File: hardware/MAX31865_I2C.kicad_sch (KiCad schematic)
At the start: 38 parts, among them J1 Conn_01x08, J2 AVR-ISP-6, J3 Conn_02x04_Odd_Even, J4 Conn_02x04_Odd_Even, J5 Conn_02x02_Odd_Even, U1 ATmega48A-A, Y1 16MHz

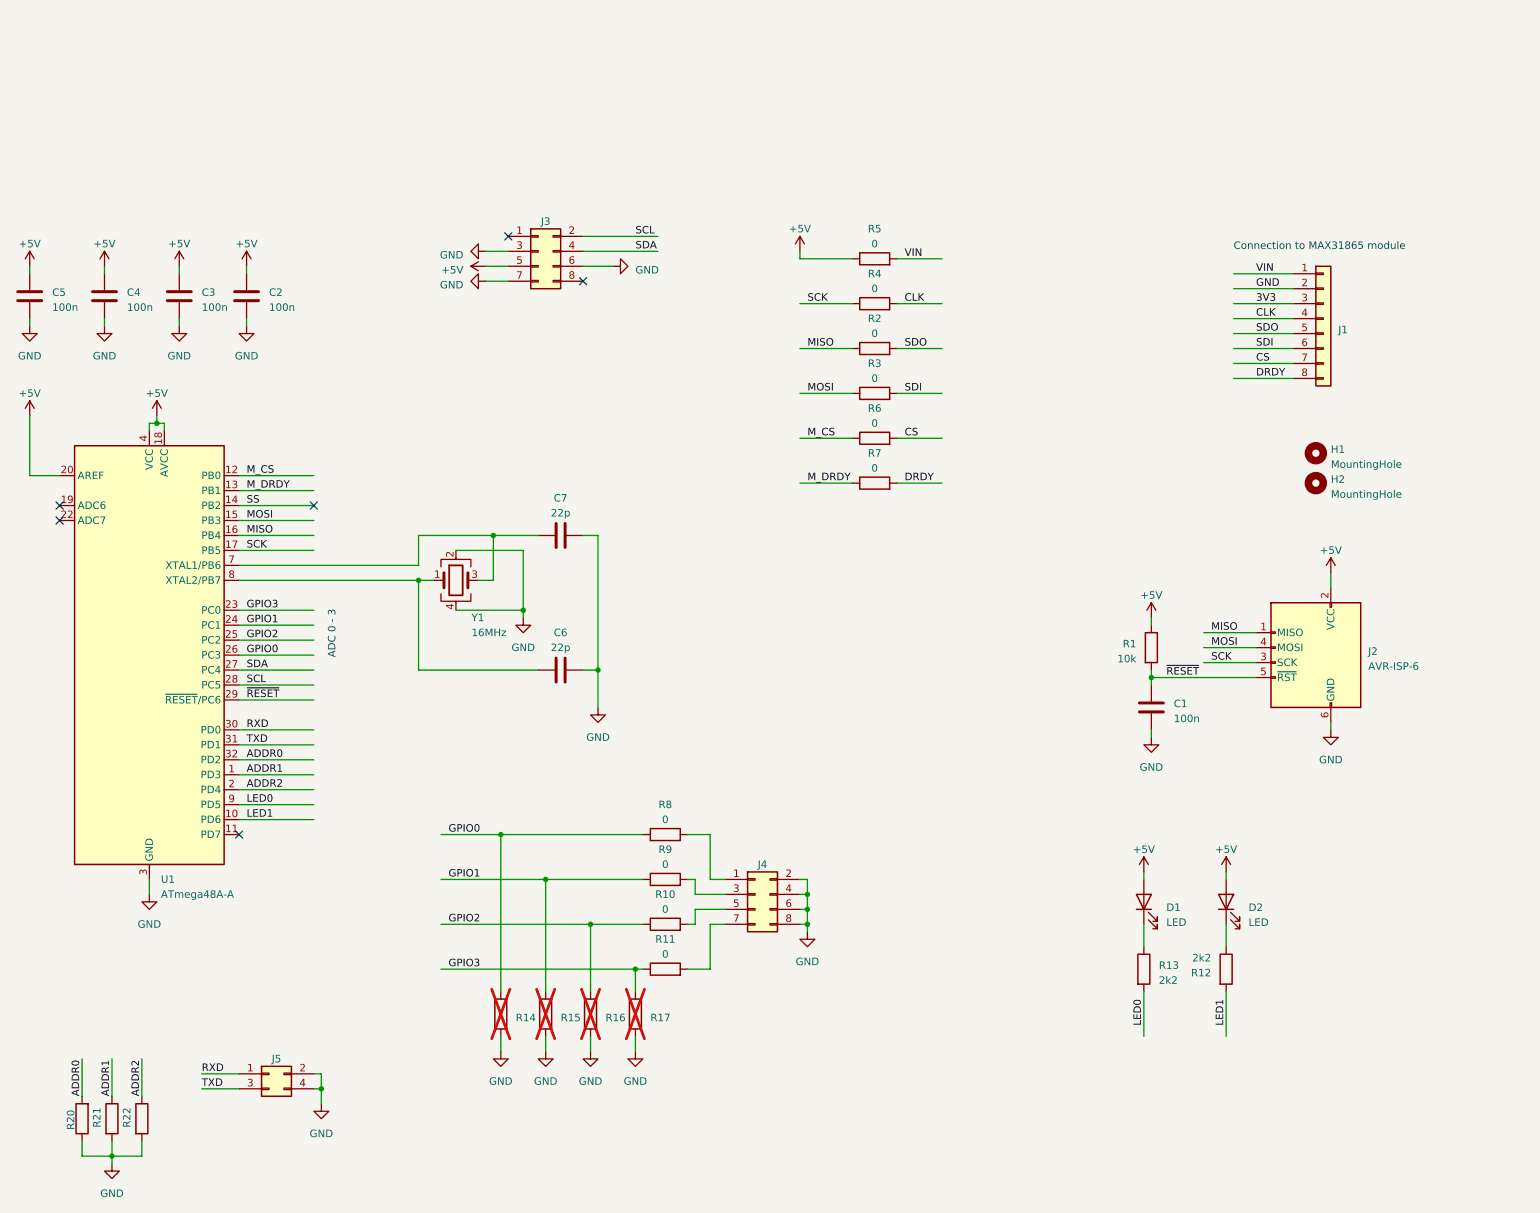
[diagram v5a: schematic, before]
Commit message: added some comments to schematic
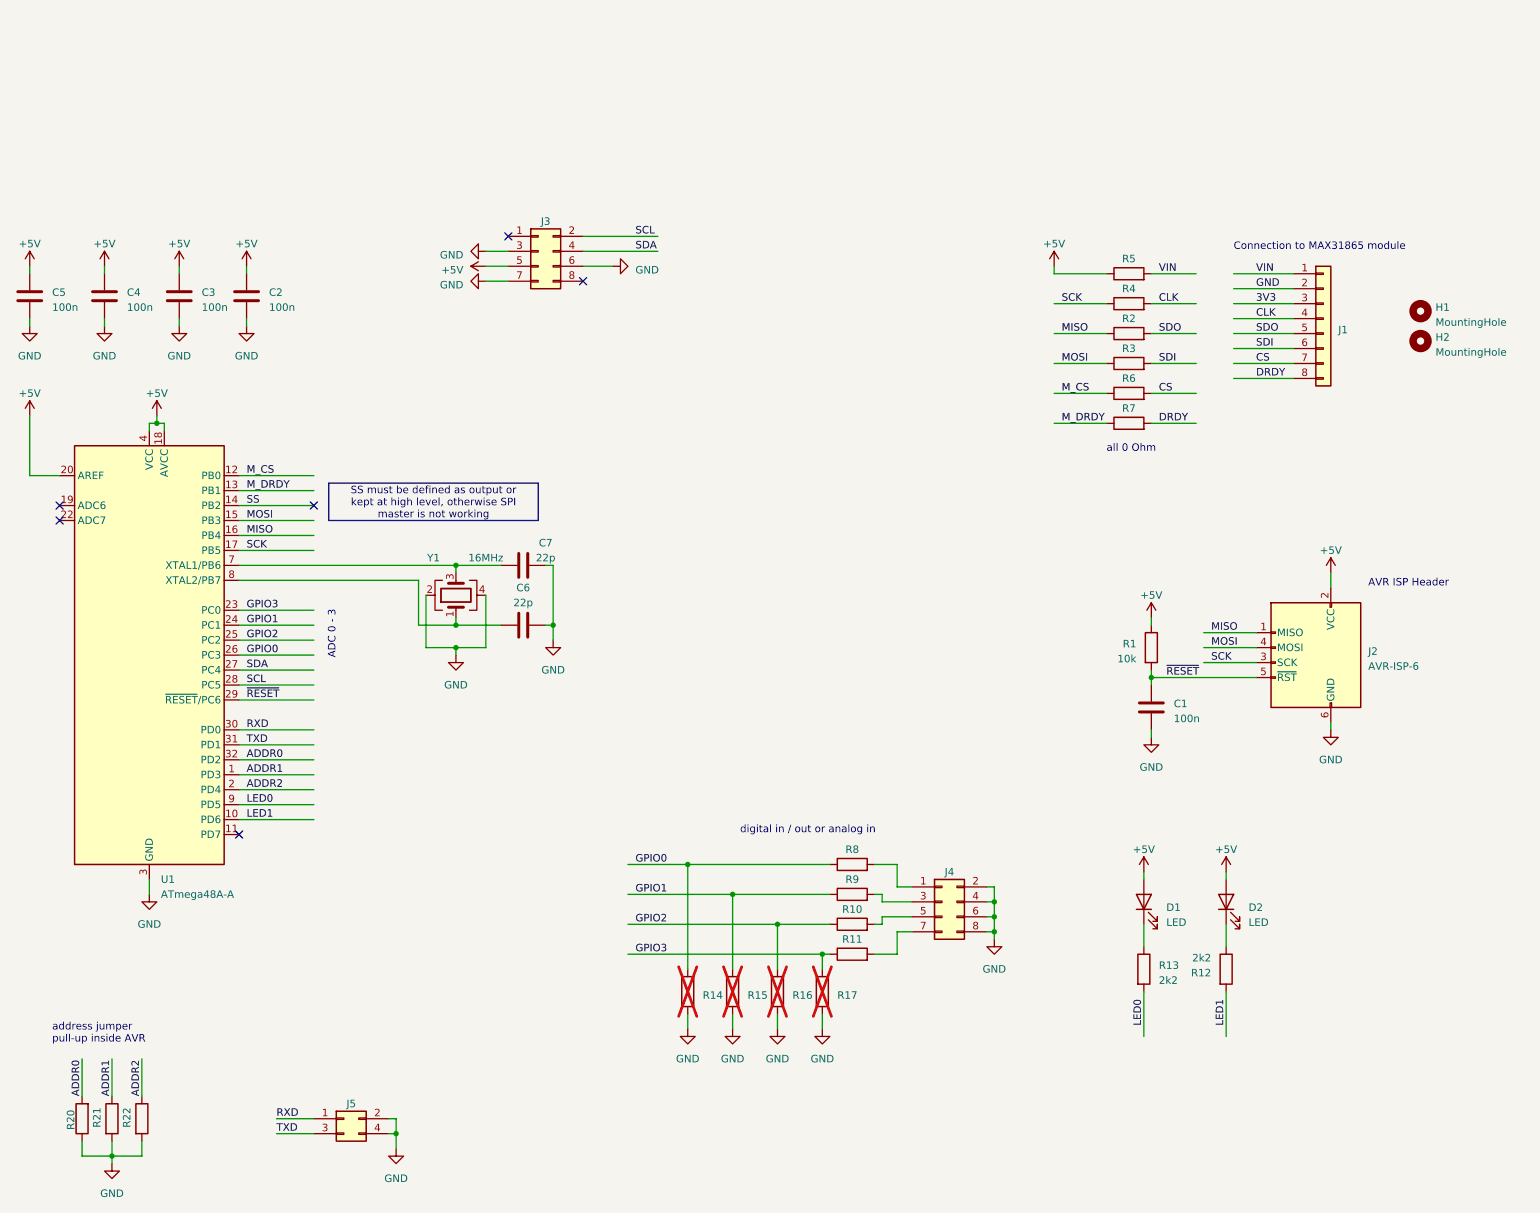
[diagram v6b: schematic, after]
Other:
- note added: "AVR ISP Header"
- note added: "address jumper pull-up inside AVR"
- note added: "all 0 Ohm"
- note added: "digital in / out or analog in"
- moved on the sheet: C6, C7, H1, H2, J4, J5, R10, R11, R14, R15, R16, R17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

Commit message: added further comments
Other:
- note added: "I2C Bus connector"
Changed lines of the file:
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@@
     (stroke (width 0) (type default))
+  )
+  (rectangle (start 209.55 21.59) (end 217.17 53.34)
+    (stroke (width -0.0001) (type default))
+    (fill (type color) (color 0 194 0 0.3))
   )
   (text_box "SS must be defined as output or kept at high level, otherwise SPI master is not working"
@@
     (effects (font (size 1.27 1.27)) (justify left bottom))
   )
-  (text "all 0 Ohm" (at 209.55 55.88 0)
+  (text "I2C Bus connector" (at 106.68 33.02 0)
     (effects (font (size 1.27 1.27)) (justify left bottom))
   )
+  (text "all 0 Ohm" (at 208.28 55.88 0)
+    (effects (font (size 1.27 1.27)) (justify left bottom))
+  )

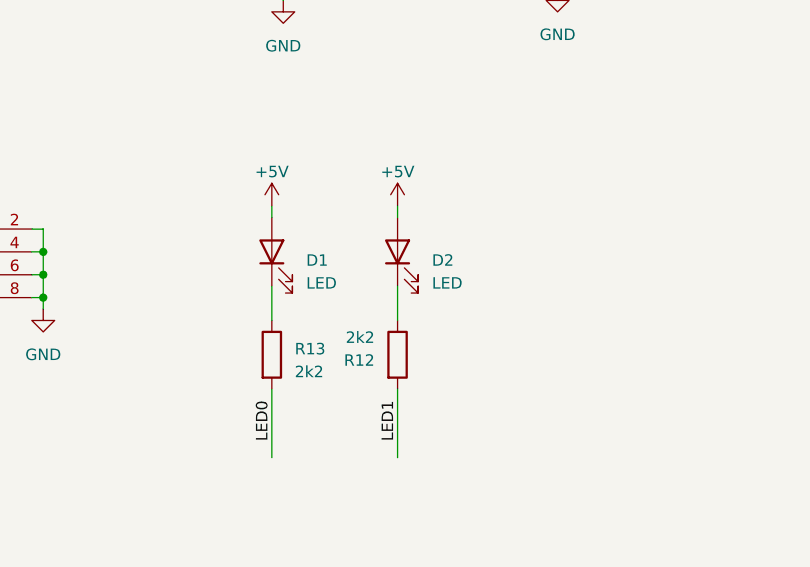
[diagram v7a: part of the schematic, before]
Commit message: tiny update to schematic and pcb
updated to KiCAD v7 release version
updated version in PCB
updated LED colors
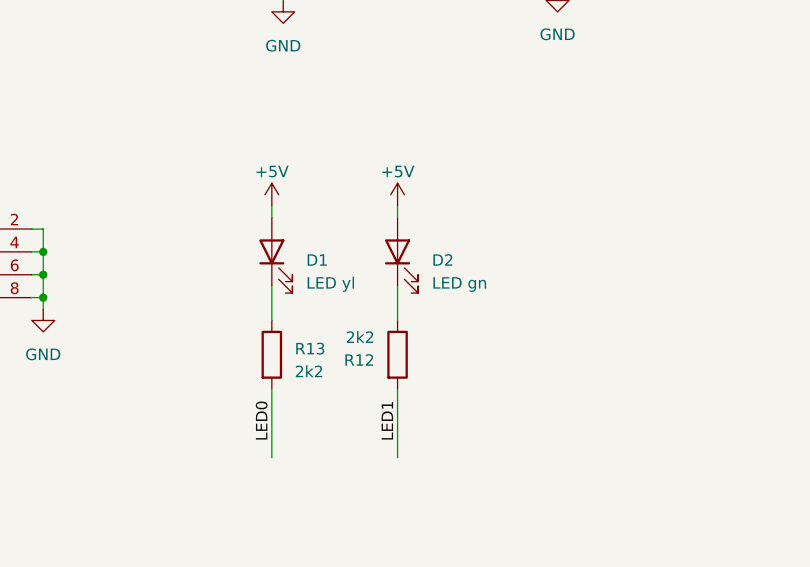
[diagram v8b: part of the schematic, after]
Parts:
- D1: value LED -> LED yl
- D2: value LED -> LED gn
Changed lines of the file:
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@@
-(kicad_sch (version 20221206) (generator eeschema)
+(kicad_sch (version 20230121) (generator eeschema)
   (paper "A4")
   (title_block
@@
       (effects (font (size 1.27 1.27)) (justify right))
     )
-    (property "Value" "LED" (at 233.68 135.5725 90)
+    (property "Value" "LED gn" (at 233.68 135.5725 90)
       (effects (font (size 1.27 1.27)) (justify right))
     )
@@
       (effects (font (size 1.27 1.27)) (justify right))
     )
-    (property "Value" "LED" (at 219.71 135.5725 90)
+    (property "Value" "LED yl" (at 219.71 135.5725 90)
       (effects (font (size 1.27 1.27)) (justify right))
     )
